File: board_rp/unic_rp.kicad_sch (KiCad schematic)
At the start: 193 parts, among them J1 SM03B-SRSS-TB, P1 USB_C_Plug_USB2.0, Q1 2N7002, Q10 2N7002, Q11 2N7002, Q12 2N7002, Q13 2N7002, Q14 2N7002, Q15 2N7002, Q16 2N7002, Q17 2N7002, Q18 2N7002, Q19 2N7002, Q2 2N7002, Q20 2N7002, Q21 2N7002, Q22 2N7002, Q23 2N7002, Q24 2N7002, Q25 2N7002, Q26 2N7002, Q27 2N7002, Q28 2N7002, Q29 2N7002, Q3 2N7002, Q30 2N7002, Q31 2N7002, Q32 2N7002, Q33 2N7002, Q34 2N7002, Q35 2N7002, Q36 2N7002, Q37 2N7002, Q38 2N7002, Q39 2N7002, Q4 2N7002, Q40 2N7002, Q41 2N7002, Q5 2N7002, Q6 2N7002, Q7 2N7002, Q8 2N7002, Q9 2N7002, U1 RP2350_80QFN, U3 MIC5203-3.3BM5, U4 APS6404L-3SQR-ZR, U6 AP62150Z6, U7 W25Q16JVUXIQ, X1 27MHz

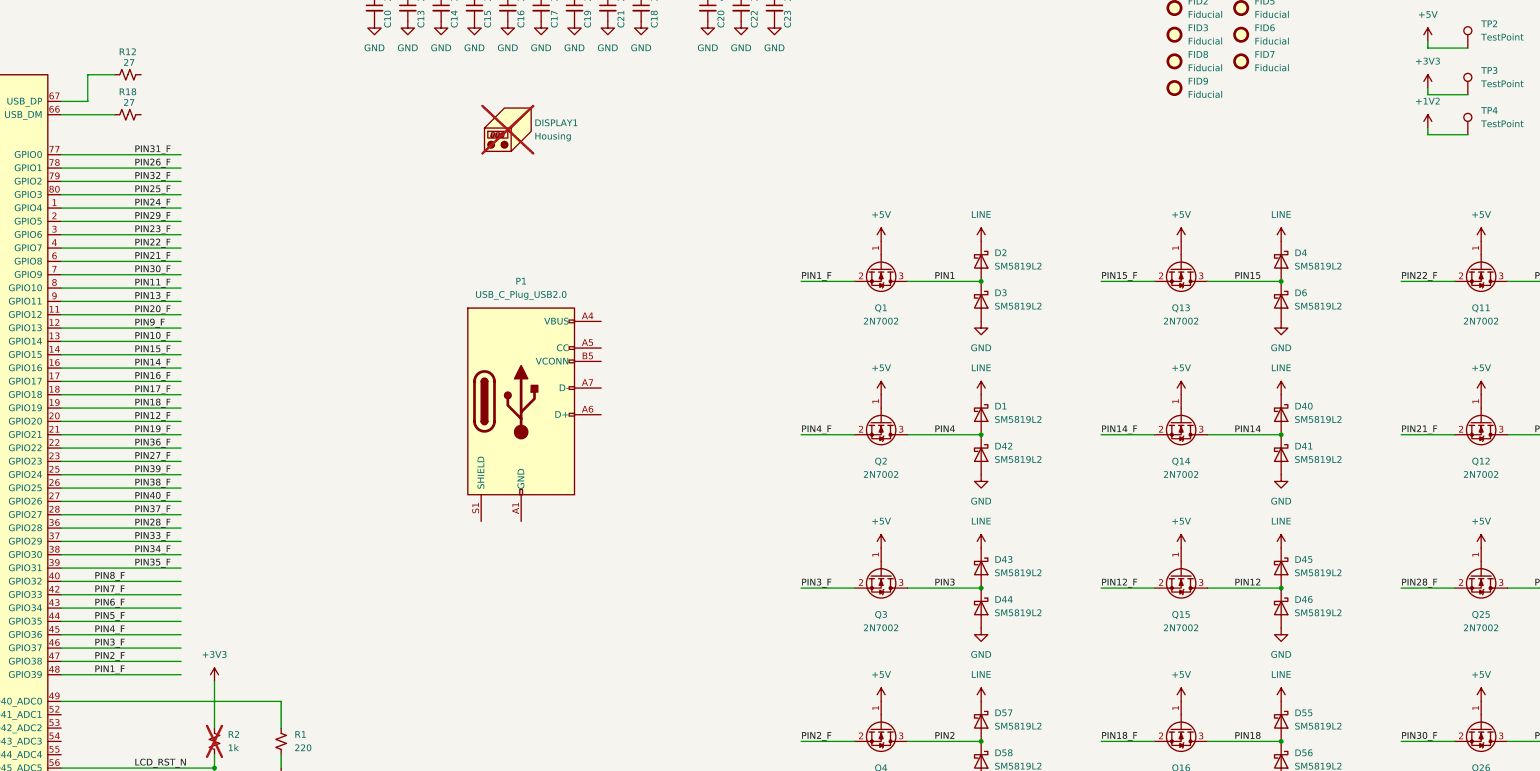
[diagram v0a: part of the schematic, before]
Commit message: More work towards RP based UnIC
The IO connections are mostly figured out, component placement
as well. Still need new inductor, proper XTAL, USB and of course
a lot of routing, including power.
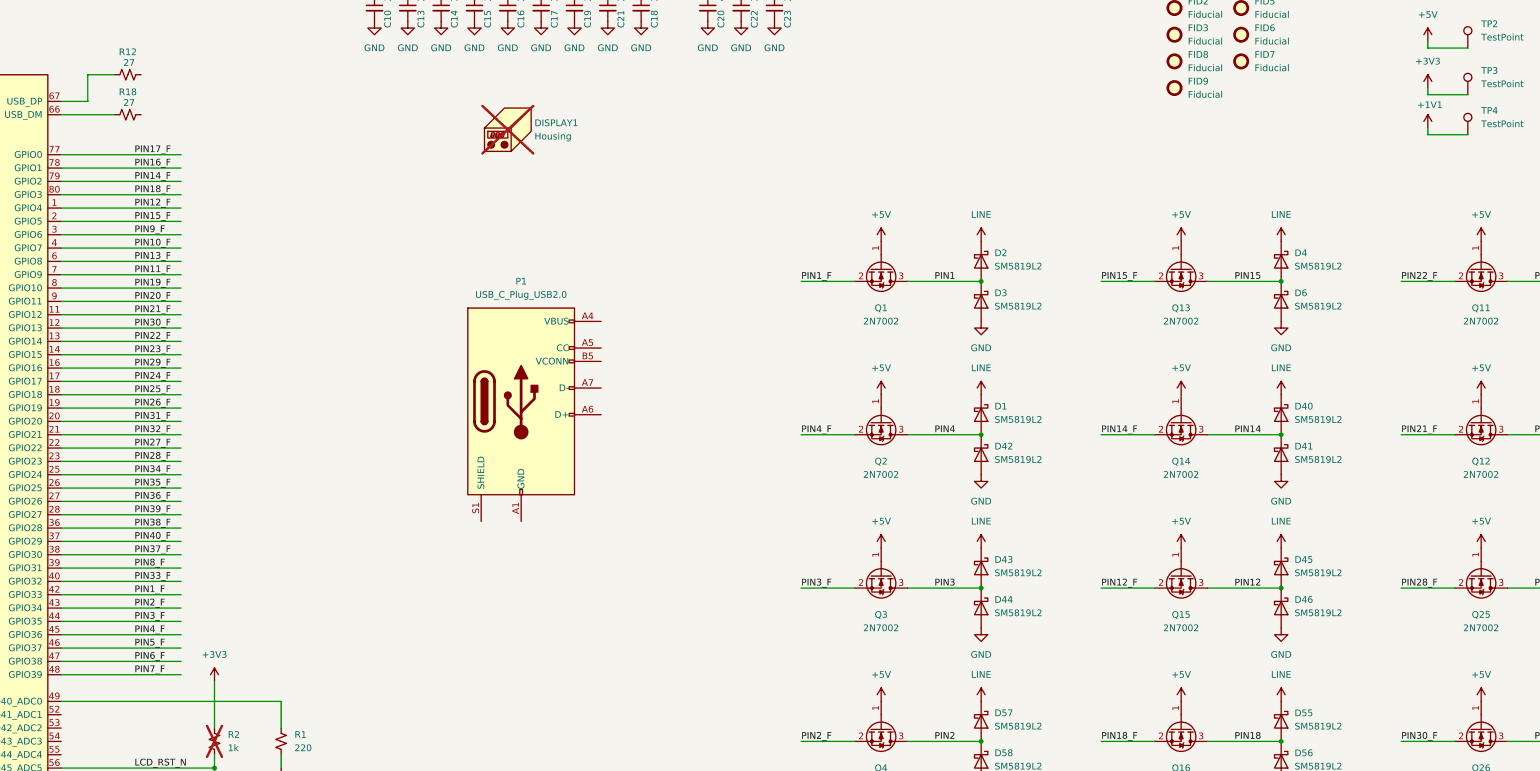
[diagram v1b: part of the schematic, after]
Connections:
- net +1V2 is gone; now on net +1V1: TP4.1
- net PIN10_F: now also U1.4 (GPIO7); no longer U1.13 (GPIO14)
- net PIN11_F: now also U1.7 (GPIO9); no longer U1.8 (GPIO10)
- net PIN12_F: now also U1.1 (GPIO4); no longer U1.20 (GPIO20)
- net PIN13_F: now also U1.6 (GPIO8); no longer U1.9 (GPIO11)
- net PIN14_F: now also U1.79 (GPIO2); no longer U1.16 (GPIO16)
- net PIN15_F: now also U1.2 (GPIO5); no longer U1.14 (GPIO15)
- net PIN16_F: now also U1.78 (GPIO1); no longer U1.17 (GPIO17)
- net PIN17_F: now also U1.77 (GPIO0); no longer U1.18 (GPIO18)
- net PIN18_F: now also U1.80 (GPIO3); no longer U1.19 (GPIO19)
- net PIN19_F: now also U1.8 (GPIO10); no longer U1.21 (GPIO21)
- net PIN1_F: now also U1.42 (GPIO33); no longer U1.48 (GPIO39)
- net PIN20_F: now also U1.9 (GPIO11); no longer U1.11 (GPIO12)
- net PIN21_F: now also U1.11 (GPIO12); no longer U1.6 (GPIO8)
- net PIN22_F: now also U1.13 (GPIO14); no longer U1.4 (GPIO7)
- net PIN23_F: now also U1.14 (GPIO15); no longer U1.3 (GPIO6)
- net PIN24_F: now also U1.17 (GPIO17); no longer U1.1 (GPIO4)
- net PIN25_F: now also U1.18 (GPIO18); no longer U1.80 (GPIO3)
- net PIN26_F: now also U1.19 (GPIO19); no longer U1.78 (GPIO1)
- net PIN27_F: now also U1.22 (GPIO22); no longer U1.23 (GPIO23)
- net PIN28_F: now also U1.23 (GPIO23); no longer U1.36 (GPIO28)
- net PIN29_F: now also U1.16 (GPIO16); no longer U1.2 (GPIO5)
- net PIN2_F: now also U1.43 (GPIO34); no longer U1.47 (GPIO38)
- net PIN30_F: now also U1.12 (GPIO13); no longer U1.7 (GPIO9)
- net PIN31_F: now also U1.20 (GPIO20); no longer U1.77 (GPIO0)
- net PIN32_F: now also U1.21 (GPIO21); no longer U1.79 (GPIO2)
- net PIN33_F: now also U1.40 (GPIO32); no longer U1.37 (GPIO29)
- net PIN34_F: now also U1.25 (GPIO24); no longer U1.38 (GPIO30)
- net PIN35_F: now also U1.26 (GPIO25); no longer U1.39 (GPIO31)
- net PIN36_F: now also U1.27 (GPIO26); no longer U1.22 (GPIO22)
- net PIN37_F: now also U1.38 (GPIO30); no longer U1.28 (GPIO27)
- net PIN38_F: now also U1.36 (GPIO28); no longer U1.26 (GPIO25)
- net PIN39_F: now also U1.28 (GPIO27); no longer U1.25 (GPIO24)
- net PIN3_F: now also U1.44 (GPIO35); no longer U1.46 (GPIO37)
- net PIN40_F: now also U1.37 (GPIO29); no longer U1.27 (GPIO26)
- net PIN5_F: now also U1.46 (GPIO37); no longer U1.44 (GPIO35)
- net PIN6_F: now also U1.47 (GPIO38); no longer U1.43 (GPIO34)
- net PIN7_F: now also U1.48 (GPIO39); no longer U1.42 (GPIO33)
- net PIN8_F: now also U1.39 (GPIO31); no longer U1.40 (GPIO32)
- net PIN9_F: now also U1.3 (GPIO6); no longer U1.12 (GPIO13)
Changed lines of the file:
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@@
 	)
 	(label "PIN23_F"
-		(at 181.61 91.44 0)
+		(at 181.61 114.3 0)
 		(fields_autoplaced yes)
 		(effects
@@
 	)
 	(label "PIN26_F"
-		(at 181.61 78.74 0)
+		(at 181.61 124.46 0)
 		(fields_autoplaced yes)
 		(effects
@@
 	)
 	(label "PIN37_F"
-		(at 181.61 144.78 0)
+		(at 181.61 152.4 0)
 		(fields_autoplaced yes)
 		(effects
@@
 	)
 	(label "PIN16_F"
-		(at 181.61 119.38 0)
+		(at 181.61 78.74 0)
 		(fields_autoplaced yes)
 		(effects
@@
 	)
 	(label "PIN13_F"
-		(at 181.61 104.14 0)
+		(at 181.61 96.52 0)
 		(fields_autoplaced yes)
 		(effects
@@
 	)
 	(label "PIN14_F"
-		(at 181.61 116.84 0)
+		(at 181.61 81.28 0)
 		(fields_autoplaced yes)
 		(effects
@@
 	)
 	(label "PIN11_F"
-		(at 181.61 101.6 0)
+		(at 181.61 99.06 0)
 		(fields_autoplaced yes)
 		(effects
@@
 	)
 	(label "PIN10_F"
-		(at 181.61 111.76 0)
+		(at 181.61 93.98 0)
 		(fields_autoplaced yes)
 		(effects
@@
 	)
 	(label "PIN12_F"
-		(at 181.61 127 0)
+		(at 181.61 86.36 0)
 		(fields_autoplaced yes)
 		(effects
@@
 	)
 	(label "PIN31_F"
-		(at 181.61 76.2 0)
+		(at 181.61 127 0)
 		(fields_autoplaced yes)
 		(effects
@@
 	)
 	(label "PIN32_F"
-		(at 181.61 81.28 0)
+		(at 181.61 129.54 0)
 		(fields_autoplaced yes)
 		(effects
@@
 	)
 	(label "PIN7_F"
-		(at 173.99 160.02 0)
+		(at 181.61 175.26 0)
 		(fields_autoplaced yes)
 		(effects
@@
 	)
 	(label "PIN39_F"
-		(at 181.61 137.16 0)
+		(at 181.61 144.78 0)
 		(fields_autoplaced yes)
 		(effects
@@
 	)
 	(label "PIN19_F"
-		(at 181.61 129.54 0)
+		(at 181.61 101.6 0)
 		(fields_autoplaced yes)
 		(effects
@@
 	)
 	(label "PIN22_F"
-		(at 181.61 93.98 0)
+		(at 181.61 111.76 0)
 		(fields_autoplaced yes)
 		(effects
@@
 	)
 	(label "PIN24_F"
-		(at 181.61 86.36 0)
+		(at 181.61 119.38 0)
 		(fields_autoplaced yes)
 		(effects
@@
 	)
 	(label "PIN18_F"
-		(at 181.61 124.46 0)
+		(at 181.61 83.82 0)
 		(fields_autoplaced yes)
 		(effects
@@
 	)
 	(label "PIN30_F"
-		(at 181.61 99.06 0)
+		(at 181.61 109.22 0)
 		(fields_autoplaced yes)
 		(effects
@@
 	)
 	(label "PIN6_F"
-		(at 173.99 162.56 0)
+		(at 181.61 172.72 0)
 		(fields_autoplaced yes)
 		(effects
@@
 	)
 	(label "PIN20_F"
-		(at 181.61 106.68 0)
+		(at 181.61 104.14 0)
 		(fields_autoplaced yes)
 		(effects
@@
 	)
 	(label "PIN29_F"
-		(at 181.61 88.9 0)
+		(at 181.61 116.84 0)
 		(fields_autoplaced yes)
 		(effects
@@
 	)
 	(label "PIN40_F"
-		(at 181.61 142.24 0)
+		(at 181.61 149.86 0)
 		(fields_autoplaced yes)
 		(effects
@@
 	)
 	(label "PIN33_F"
-		(at 181.61 149.86 0)
+		(at 181.61 157.48 0)
 		(fields_autoplaced yes)
 		(effects
@@
 	)
 	(label "PIN27_F"
-		(at 181.61 134.62 0)
+		(at 181.61 132.08 0)
 		(fields_autoplaced yes)
 		(effects
@@
 	)
 	(label "PIN34_F"
-		(at 181.61 152.4 0)
+		(at 181.61 137.16 0)
 		(fields_autoplaced yes)
 		(effects
@@
 	)
 	(label "PIN1_F"
-		(at 173.99 175.26 0)
+		(at 181.61 160.02 0)
 		(fields_autoplaced yes)
 		(effects
@@
 	)
 	(label "PIN38_F"
-		(at 181.61 139.7 0)
+		(at 181.61 147.32 0)
 		(fields_autoplaced yes)
 		(effects
@@
 	)
 	(label "PIN5_F"
-		(at 173.99 165.1 0)
+		(at 181.61 170.18 0)
 		(fields_autoplaced yes)
 		(effects
@@
 	)
 	(label "PIN35_F"
-		(at 181.61 154.94 0)
+		(at 181.61 139.7 0)
 		(fields_autoplaced yes)
 		(effects
@@
 	)
 	(label "PIN21_F"
-		(at 181.61 96.52 0)
+		(at 181.61 106.68 0)
 		(fields_autoplaced yes)
 		(effects
@@
 	)
 	(label "PIN2_F"
-		(at 173.99 172.72 0)
+		(at 181.61 162.56 0)
 		(fields_autoplaced yes)
 		(effects
@@
 	)
 	(label "PIN25_F"
-		(at 181.61 83.82 0)
+		(at 181.61 121.92 0)
 		(fields_autoplaced yes)
 		(effects
@@
 	)
 	(label "PIN9_F"
-		(at 181.61 109.22 0)
+		(at 181.61 91.44 0)
 		(fields_autoplaced yes)
 		(effects
@@
 	)
 	(label "PIN3_F"
-		(at 173.99 170.18 0)
+		(at 181.61 165.1 0)
 		(fields_autoplaced yes)
 		(effects
@@
 	)
 	(label "PIN8_F"
-		(at 173.99 157.48 0)
+		(at 181.61 154.94 0)
 		(fields_autoplaced yes)
 		(effects
@@
 	)
 	(label "PIN4_F"
-		(at 173.99 167.64 0)
+		(at 181.61 167.64 0)
 		(fields_autoplaced yes)
 		(effects
@@
 	)
 	(label "PIN36_F"
-		(at 181.61 132.08 0)
+		(at 181.61 142.24 0)
 		(fields_autoplaced yes)
 		(effects
@@
 	)
 	(label "PIN15_F"
-		(at 181.61 114.3 0)
+		(at 181.61 88.9 0)
 		(fields_autoplaced yes)
 		(effects
@@
 	)
 	(label "PIN28_F"
-		(at 181.61 147.32 0)
+		(at 181.61 134.62 0)
 		(fields_autoplaced yes)
 		(effects
@@
 	)
 	(label "PIN17_F"
-		(at 181.61 121.92 0)
+		(at 181.61 76.2 0)
 		(fields_autoplaced yes)
 		(effects
@@
 	)
 	(symbol
+		(lib_id "power:+1V1")
+		(at 427.99 71.12 0)
+		(unit 1)
+		(exclude_from_sim no)
+		(in_bom yes)
+		(on_board yes)
+		(dnp no)
+		(property "Reference" "#PWR020"
+			(at 427.99 74.93 0)
+			(effects
+				(font
+					(size 1.27 1.27)
+				)
+				(hide yes)
+			)
+		)
+		(property "Value" "+1V1"
+			(at 428.371 66.7258 0)
+			(effects
+				(font
+					(size 1.27 1.27)
+				)
+			)
+		)
+		(property "Footprint" ""
+			(at 427.99 71.12 0)
+			(effects
+				(font
+					(size 1.27 1.27)
+				)
+				(hide yes)
+			)
+		)
+		(property "Datasheet" ""
+			(at 427.99 71.12 0)
+			(effects
+				(font
+					(size 1.27 1.27)
+				)
+				(hide yes)
+			)
+		)
+		(property "Description" ""
+			(at 427.99 71.12 0)
+			(effects
+				(font
+					(size 1.27 1.27)
+				)
+				(hide yes)
+			)
+		)
+		(pin "1"
+		)
+		(instances
+			(project "unic_rp"
+				(path "/f6df1e3b-3728-4bb2-8d84-c5251d58c11a"
+					(reference "#PWR020")
+					(unit 1)
+				)
+			)
+		)
+	)
+	(symbol
 		(lib_id "Transistor_FET:2N7002")
 		(at 496.57 243.84 270)
@@
 					(unit 1)
 				)
-			)
-		)
-	)
-	(symbol
-		(lib_id "power:+1V2")
-		(at 427.99 71.12 0)
-		(unit 1)
-		(exclude_from_sim no)
-		(in_bom yes)
-		(on_board yes)
-		(dnp no)
-		(fields_autoplaced yes)
-		(property "Reference" "#PWR020"
-			(at 427.99 74.93 0)
-			(effects
-				(font
-					(size 1.27 1.27)
-				)
-				(hide yes)
-			)
-		)
-		(property "Value" "+1V2"
-			(at 427.99 66.04 0)
-			(effects
-				(font
-					(size 1.27 1.27)
-				)
-			)
-		)
-		(property "Footprint" ""
-			(at 427.99 71.12 0)
-			(effects
-				(font
-					(size 1.27 1.27)
-				)
-				(hide yes)
-			)
-		)
-		(property "Datasheet" ""
-			(at 427.99 71.12 0)
-			(effects
-				(font
-					(size 1.27 1.27)
-				)
-				(hide yes)
-			)
-		)
-		(property "Description" ""
-			(at 427.99 71.12 0)
-			(effects
-				(font
-					(size 1.27 1.27)
-				)
-				(hide yes)
-			)
-		)
-		(pin "1"
-		)
-		(instances
-			(project "unic_gw1"
-				(path "/f6df1e3b-3728-4bb2-8d84-c5251d58c11a"
-					(reference "#PWR020")
-					(unit 1)
-				)
